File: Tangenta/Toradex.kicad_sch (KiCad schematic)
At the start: 24 parts, among them J17 2309410-1, J30 Conn_01x02_Pin, J31 Conn_01x09_Pin, J32 Conn_02x03_Odd_Even, J33 Conn_01x05_Pin, J34 Conn_01x05_Pin, Q3 BSS138, T1 NTZD3154NT1G

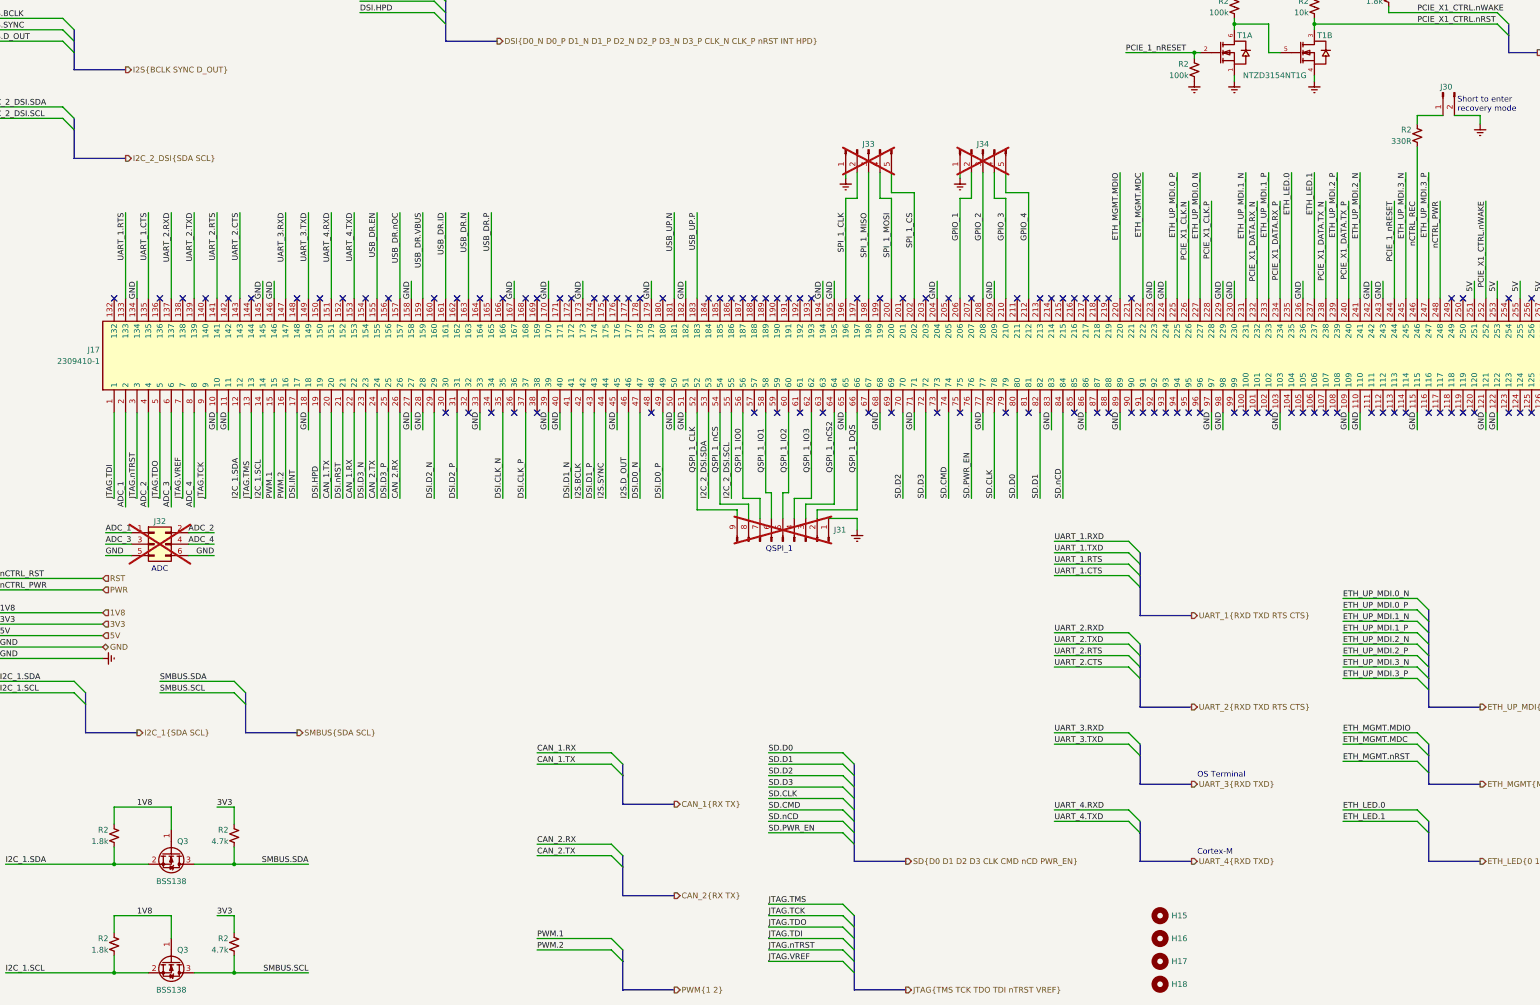
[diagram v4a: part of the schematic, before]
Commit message: Re-annotated. Ready for JLCPCB design verification.
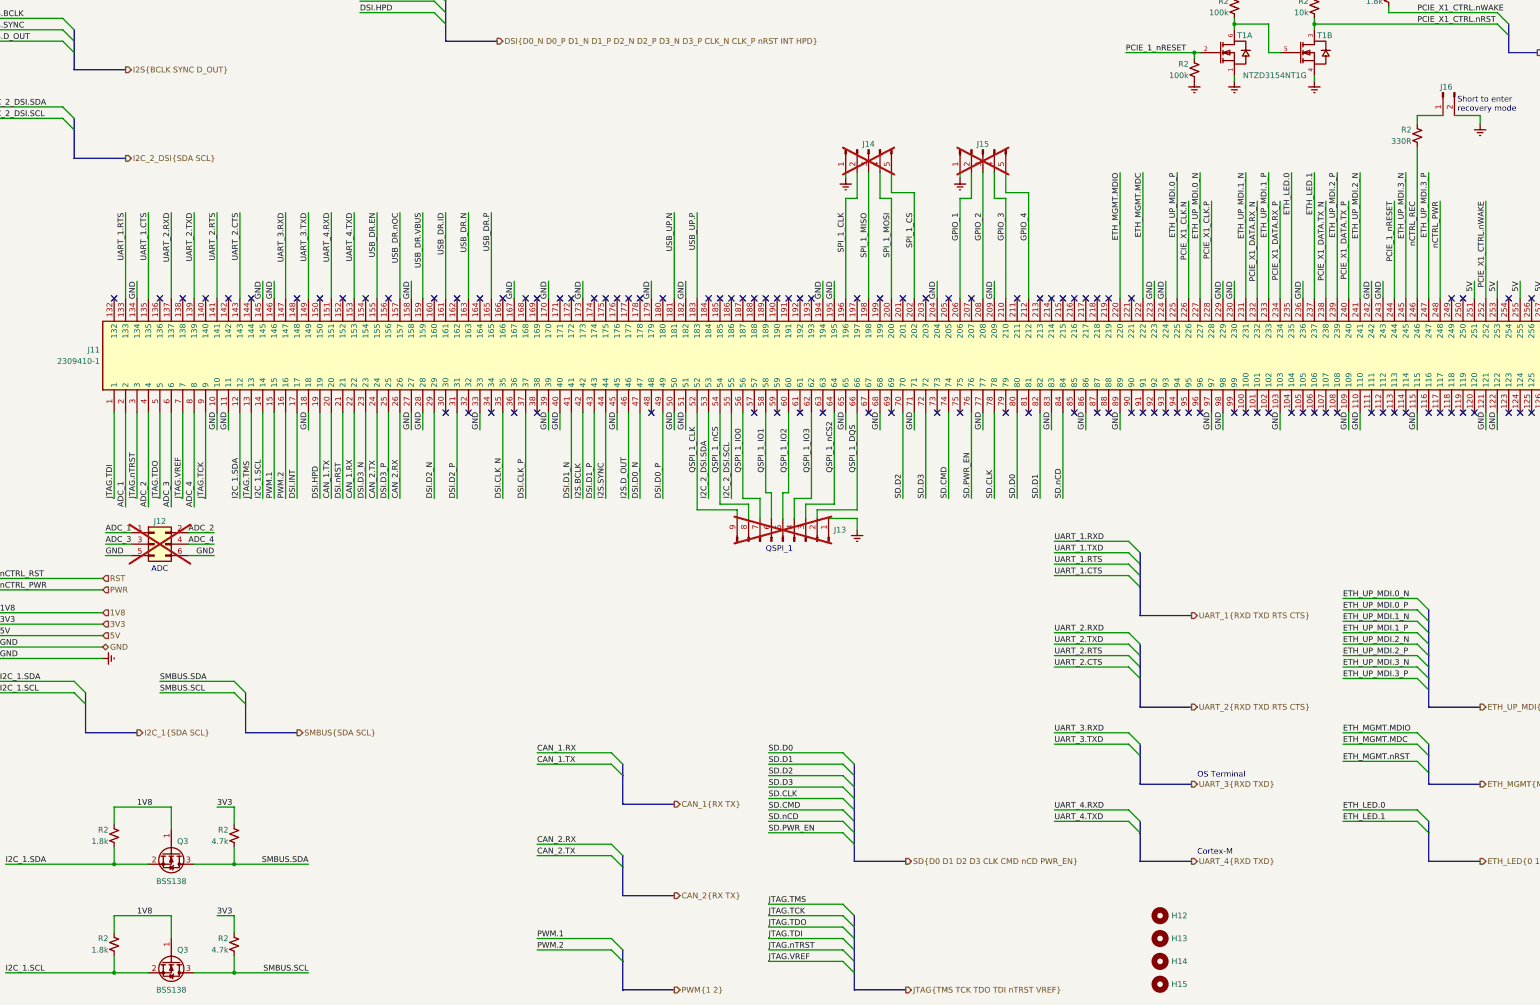
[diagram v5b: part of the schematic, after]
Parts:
- renumbered H15 to H12, H16 to H13, H17 to H14, H18 to H15, J17 to J11, J32 to J12, J31 to J13, J33 to J14, J34 to J15, J30 to J16
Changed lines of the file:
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@@
         )
         (path "/358d1bcf-7599-4352-8c4d-baa18a5f09e6/db297b0b-35f2-4e86-892c-83973f1ac2db"
-          (reference "R54") (unit 1)
+          (reference "R74") (unit 1)
         )
       )
@@
   (symbol (lib_id "CholaSymbolsPrjLib:MountingHole") (at 281.94 260.35 0) (unit 1)
     (in_bom yes) (on_board yes) (dnp no)
-    (property "Reference" "H15" (at 284.48 260.35 0)
+    (property "Reference" "H12" (at 284.48 260.35 0)
       (effects (font (size 1.27 1.27)) (justify left))
     )
@@
       (project "Tangenta"
         (path "/358d1bcf-7599-4352-8c4d-baa18a5f09e6/db297b0b-35f2-4e86-892c-83973f1ac2db"
-          (reference "H15") (unit 1)
+          (reference "H12") (unit 1)
         )
       )
@@
         )
         (path "/358d1bcf-7599-4352-8c4d-baa18a5f09e6/db297b0b-35f2-4e86-892c-83973f1ac2db"
-          (reference "Q5") (unit 1)
+          (reference "Q9") (unit 1)
         )
       )
@@
         )
         (path "/358d1bcf-7599-4352-8c4d-baa18a5f09e6/db297b0b-35f2-4e86-892c-83973f1ac2db"
-          (reference "#PWR0109") (unit 1)
+          (reference "#PWR063") (unit 1)
         )
       )
@@
   (symbol (lib_id "CholaSymbolsPrjLib:MountingHole") (at 281.94 275.59 0) (unit 1)
     (in_bom yes) (on_board yes) (dnp no)
-    (property "Reference" "H18" (at 284.48 275.59 0)
+    (property "Reference" "H15" (at 284.48 275.59 0)
       (effects (font (size 1.27 1.27)) (justify left))
     )
@@
       (project "Tangenta"
         (path "/358d1bcf-7599-4352-8c4d-baa18a5f09e6/db297b0b-35f2-4e86-892c-83973f1ac2db"
-          (reference "H18") (unit 1)
+          (reference "H15") (unit 1)
         )
       )
@@
         )
         (path "/358d1bcf-7599-4352-8c4d-baa18a5f09e6/db297b0b-35f2-4e86-892c-83973f1ac2db"
-          (reference "#PWR0111") (unit 1)
+          (reference "#PWR064") (unit 1)
         )
       )
@@
         )
         (path "/358d1bcf-7599-4352-8c4d-baa18a5f09e6/db297b0b-35f2-4e86-892c-83973f1ac2db"
-          (reference "R41") (unit 1)
+          (reference "R70") (unit 1)
         )
       )
@@
   (symbol (lib_id "CholaSymbolsPrjLib:Conn_01x02_Pin") (at 344.805 77.47 90) (mirror x) (unit 1)
     (in_bom yes) (on_board yes) (dnp no)
-    (property "Reference" "J30" (at 344.17 76.2 90)
+    (property "Reference" "J16" (at 344.17 76.2 90)
       (effects (font (size 1.27 1.27)) (justify right))
     )
@@
       (project "Tangenta"
         (path "/358d1bcf-7599-4352-8c4d-baa18a5f09e6/db297b0b-35f2-4e86-892c-83973f1ac2db"
-          (reference "J30") (unit 1)
+          (reference "J16") (unit 1)
         )
       )
@@
         )
         (path "/358d1bcf-7599-4352-8c4d-baa18a5f09e6/db297b0b-35f2-4e86-892c-83973f1ac2db"
-          (reference "#PWR056") (unit 1)
+          (reference "#PWR066") (unit 1)
         )
       )
@@
   (symbol (lib_id "CholaSymbolsPrjLib:MountingHole") (at 281.94 265.43 0) (unit 1)
     (in_bom yes) (on_board yes) (dnp no)
-    (property "Reference" "H16" (at 284.48 265.43 0)
+    (property "Reference" "H13" (at 284.48 265.43 0)
       (effects (font (size 1.27 1.27)) (justify left))
     )
@@
       (project "Tangenta"
         (path "/358d1bcf-7599-4352-8c4d-baa18a5f09e6/db297b0b-35f2-4e86-892c-83973f1ac2db"
-          (reference "H16") (unit 1)
+          (reference "H13") (unit 1)
         )
       )
@@
   (symbol (lib_id "CholaSymbolsPrjLib:2309410-1") (at 49.53 148.59 90) (unit 1)
     (in_bom yes) (on_board yes) (dnp no) (fields_autoplaced)
-    (property "Reference" "J17" (at 46.355 134.62 90)
+    (property "Reference" "J11" (at 46.355 134.62 90)
       (effects (font (size 1.27 1.27)) (justify left))
     )
@@
       (project "Tangenta"
         (path "/358d1bcf-7599-4352-8c4d-baa18a5f09e6/db297b0b-35f2-4e86-892c-83973f1ac2db"
-          (reference "J17") (unit 1)
+          (reference "J11") (unit 1)
         )
       )
@@
         )
         (path "/358d1bcf-7599-4352-8c4d-baa18a5f09e6/db297b0b-35f2-4e86-892c-83973f1ac2db"
-          (reference "R28") (unit 1)
+          (reference "R72") (unit 1)
         )
       )
@@
   (symbol (lib_id "CholaSymbolsPrjLib:Conn_01x09_Pin") (at 198.12 177.165 270) (mirror x) (unit 1)
     (in_bom no) (on_board yes) (dnp yes)
-    (property "Reference" "J31" (at 210.82 174.625 90)
+    (property "Reference" "J13" (at 210.82 174.625 90)
       (effects (font (size 1.27 1.27)))
     )
@@
       (project "Tangenta"
         (path "/358d1bcf-7599-4352-8c4d-baa18a5f09e6/db297b0b-35f2-4e86-892c-83973f1ac2db"
-          (reference "J31") (unit 1)
+          (reference "J13") (unit 1)
         )
       )
@@
         )
         (path "/358d1bcf-7599-4352-8c4d-baa18a5f09e6/db297b0b-35f2-4e86-892c-83973f1ac2db"
-          (reference "R42") (unit 1)
+          (reference "R71") (unit 1)
         )
       )
@@
         )
         (path "/358d1bcf-7599-4352-8c4d-baa18a5f09e6/db297b0b-35f2-4e86-892c-83973f1ac2db"
-          (reference "C219") (unit 1)
+          (reference "C106") (unit 1)
         )
       )
@@
         )
         (path "/358d1bcf-7599-4352-8c4d-baa18a5f09e6/db297b0b-35f2-4e86-892c-83973f1ac2db"
-          (reference "#PWR055") (unit 1)
+          (reference "#PWR067") (unit 1)
         )
       )
@@
   (symbol (lib_id "CholaSymbolsPrjLib:Conn_01x05_Pin") (at 217.17 90.17 90) (mirror x) (unit 1)
     (in_bom no) (on_board yes) (dnp yes)
-    (property "Reference" "J33" (at 217.17 88.9 90)
+    (property "Reference" "J14" (at 217.17 88.9 90)
       (effects (font (size 1.27 1.27)))
     )
@@
       (project "Tangenta"
         (path "/358d1bcf-7599-4352-8c4d-baa18a5f09e6/db297b0b-35f2-4e86-892c-83973f1ac2db"
-          (reference "J33") (unit 1)
+          (reference "J14") (unit 1)
         )
       )
@@
         )
         (path "/358d1bcf-7599-4352-8c4d-baa18a5f09e6/db297b0b-35f2-4e86-892c-83973f1ac2db"
-          (reference "#PWR0112") (unit 1)
+          (reference "#PWR069") (unit 1)
         )
       )
@@
         )
         (path "/358d1bcf-7599-4352-8c4d-baa18a5f09e6/db297b0b-35f2-4e86-892c-83973f1ac2db"
-          (reference "#PWR054") (unit 1)
+          (reference "#PWR065") (unit 1)
         )
       )
@@
         )
         (path "/358d1bcf-7599-4352-8c4d-baa18a5f09e6/db297b0b-35f2-4e86-892c-83973f1ac2db"
-          (reference "R55") (unit 1)
+          (reference "R75") (unit 1)
         )
       )
@@
         )
         (path "/358d1bcf-7599-4352-8c4d-baa18a5f09e6/db297b0b-35f2-4e86-892c-83973f1ac2db"
-          (reference "C220") (unit 1)
+          (reference "C107") (unit 1)
         )
       )
@@
   (symbol (lib_id "CholaSymbolsPrjLib:Conn_02x03_Odd_Even") (at 58.42 177.8 0) (unit 1)
     (in_bom no) (on_board yes) (dnp yes)
-    (property "Reference" "J32" (at 59.69 172.72 0)
+    (property "Reference" "J12" (at 59.69 172.72 0)
       (effects (font (size 1.27 1.27)))
     )
@@
       (project "Tangenta"
         (path "/358d1bcf-7599-4352-8c4d-baa18a5f09e6/db297b0b-35f2-4e86-892c-83973f1ac2db"
-          (reference "J32") (unit 1)
+          (reference "J12") (unit 1)
         )
       )
@@
         )
         (path "/358d1bcf-7599-4352-8c4d-baa18a5f09e6/db297b0b-35f2-4e86-892c-83973f1ac2db"
-          (reference "R29") (unit 1)
+          (reference "R73") (unit 1)
         )
       )
@@
         )
         (path "/358d1bcf-7599-4352-8c4d-baa18a5f09e6/db297b0b-35f2-4e86-892c-83973f1ac2db"
-          (reference "#PWR0105") (unit 1)
+          (reference "#PWR068") (unit 1)
         )
       )
@@
         )
         (path "/358d1bcf-7599-4352-8c4d-baa18a5f09e6/db297b0b-35f2-4e86-892c-83973f1ac2db"
-          (reference "Q6") (unit 1)
+          (reference "Q10") (unit 1)
         )
       )
@@
         )
         (path "/358d1bcf-7599-4352-8c4d-baa18a5f09e6/db297b0b-35f2-4e86-892c-83973f1ac2db"
-          (reference "R202") (unit 1)
+          (reference "R78") (unit 1)
         )
       )
@@
         )
         (path "/358d1bcf-7599-4352-8c4d-baa18a5f09e6/db297b0b-35f2-4e86-892c-83973f1ac2db"
-          (reference "R109") (unit 1)
+          (reference "R77") (unit 1)
         )
       )
@@
         )
         (path "/358d1bcf-7599-4352-8c4d-baa18a5f09e6/db297b0b-35f2-4e86-892c-83973f1ac2db"
-          (reference "R56") (unit 1)
+          (reference "R76") (unit 1)
         )
       )
@@
   (symbol (lib_id "CholaSymbolsPrjLib:Conn_01x05_Pin") (at 242.57 90.17 90) (mirror x) (unit 1)
     (in_bom no) (on_board yes) (dnp yes)
-    (property "Reference" "J34" (at 242.57 88.9 90)
+    (property "Reference" "J15" (at 242.57 88.9 90)
       (effects (font (size 1.27 1.27)))
     )
@@
       (project "Tangenta"
         (path "/358d1bcf-7599-4352-8c4d-baa18a5f09e6/db297b0b-35f2-4e86-892c-83973f1ac2db"
-          (reference "J34") (unit 1)
+          (reference "J15") (unit 1)
         )
       )
@@
         )
         (path "/358d1bcf-7599-4352-8c4d-baa18a5f09e6/db297b0b-35f2-4e86-892c-83973f1ac2db"
-          (reference "#PWR0110") (unit 1)
+          (reference "#PWR062") (unit 1)
         )
       )
@@
         )
         (path "/358d1bcf-7599-4352-8c4d-baa18a5f09e6/db297b0b-35f2-4e86-892c-83973f1ac2db"
-          (reference "#PWR044") (unit 1)
+          (reference "#PWR061") (unit 1)
         )
       )
@@
   (symbol (lib_id "CholaSymbolsPrjLib:MountingHole") (at 281.94 270.51 0) (unit 1)
     (in_bom yes) (on_board yes) (dnp no)
-    (property "Reference" "H17" (at 284.48 270.51 0)
+    (property "Reference" "H14" (at 284.48 270.51 0)
       (effects (font (size 1.27 1.27)) (justify left))
     )
@@
       (project "Tangenta"
         (path "/358d1bcf-7599-4352-8c4d-baa18a5f09e6/db297b0b-35f2-4e86-892c-83973f1ac2db"
-          (reference "H17") (unit 1)
-        )
-      )
+          (reference "H14") (unit 1)
+        )
+      )

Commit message: Toradex Verdin module 3Ds.
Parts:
- J11: footprint SODIMM_DDR4:SODIMM_DDR4 -> CholaFootprintsPrjLib:SODIMM_DDR4
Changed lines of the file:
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@@
       (effects (font (size 1.27 1.27)) (justify left))
     )
-    (property "Footprint" "SODIMM_DDR4:SODIMM_DDR4" (at 144.45 127 0)
+    (property "Footprint" "CholaFootprintsPrjLib:SODIMM_DDR4" (at 144.45 127 0)
       (effects (font (size 1.27 1.27)) (justify left top) hide)
     )

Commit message: initialize branch
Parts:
- renumbered C17 to C106, C17 to C107, Q3 to Q10, Q3 to Q9, R2 to R70, R2 to R71, R2 to R72, R2 to R73, R2 to R74, R2 to R75, R2 to R76, R2 to R77, R2 to R78

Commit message: CAP_L5, NTZD3154NT1G
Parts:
- C106, C107: footprint CAP_TANTAL_A:CAP_TANTAL_A -> CholaFootprintsPrjLib:CAP_TANTAL_A
- T1: footprint NTZD3154NT1G:NTZD3154NT1G -> CholaFootprintsPrjLib:NTZD3154NT1G
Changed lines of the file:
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@@
       (effects (font (size 1.27 1.27)) (justify right))
     )
-    (property "Footprint" "CAP_TANTAL_A:CAP_TANTAL_A" (at 376.301 132.842 0)
+    (property "Footprint" "CholaFootprintsPrjLib:CAP_TANTAL_A" (at 376.301 132.842 0)
       (effects (font (size 1.27 1.27) italic) hide)
     )
@@
       (effects (font (size 1.27 1.27)) (justify left))
     )
-    (property "Footprint" "NTZD3154NT1G:NTZD3154NT1G" (at 304.8 91.44 0)
+    (property "Footprint" "CholaFootprintsPrjLib:NTZD3154NT1G" (at 304.8 91.44 0)
       (effects (font (size 1.27 1.27) italic) hide)
     )
@@
     )
   )
-  (symbol (lib_id "CholaSymbolsPrjLib:NTZD3154NT1G") (at 316.23 68.58 0) (unit 2)
+  (symbol (lib_name "NTZD3154NT1G_1") (lib_id "CholaSymbolsPrjLib:NTZD3154NT1G") (at 316.23 68.58 0) (unit 2)
     (in_bom yes) (on_board yes) (dnp no)
     (property "Reference" "T1" (at 316.865 64.77 0)
@@
       (effects (font (size 1.27 1.27)) (justify left) hide)
     )
-    (property "Footprint" "NTZD3154NT1G:NTZD3154NT1G" (at 322.58 91.44 0)
+    (property "Footprint" "CholaFootprintsPrjLib:NTZD3154NT1G" (at 322.58 91.44 0)
       (effects (font (size 1.27 1.27) italic) hide)
     )
@@
     )
   )
-  (symbol (lib_id "CholaSymbolsPrjLib:CA45-A-6_3V-47UF-K") (at 398.145 135.89 270) (mirror x) (unit 1)
+  (symbol (lib_name "CA45-A-6_3V-47UF-K_1") (lib_id "CholaSymbolsPrjLib:CA45-A-6_3V-47UF-K") (at 398.145 135.89 270) (mirror x) (unit 1)
     (in_bom yes) (on_board yes) (dnp no)
     (property "Reference" "C107" (at 403.86 133.985 90)
@@
       (effects (font (size 1.27 1.27)) (justify right))
     )
-    (property "Footprint" "CAP_TANTAL_A:CAP_TANTAL_A" (at 386.461 132.842 0)
-      (effects (font (size 1.27 1.27) italic) hide)
-    )
+    (property "Footprint" "CholaFootprintsPrjLib:CAP_TANTAL_A" (at 386.461 132.842 0)
+      (effects (font (size 1.27 1.27) italic) hide)
+    )
